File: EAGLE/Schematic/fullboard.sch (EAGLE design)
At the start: 91 parts, among them CN1 B4B-XH-A, CN2 B4B-XH-A, IC1 IFX007T, IC2 IFX007T, IC3 IFX007T, IC4 IFX007T, J1 10118193-0001LF, Q1 8MHz ±10ppm Crystal 18pF 80 O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, SW1 TR1-SPST, U1 ATXMEGA128A3U-AU, U2 FT232RL-REEL

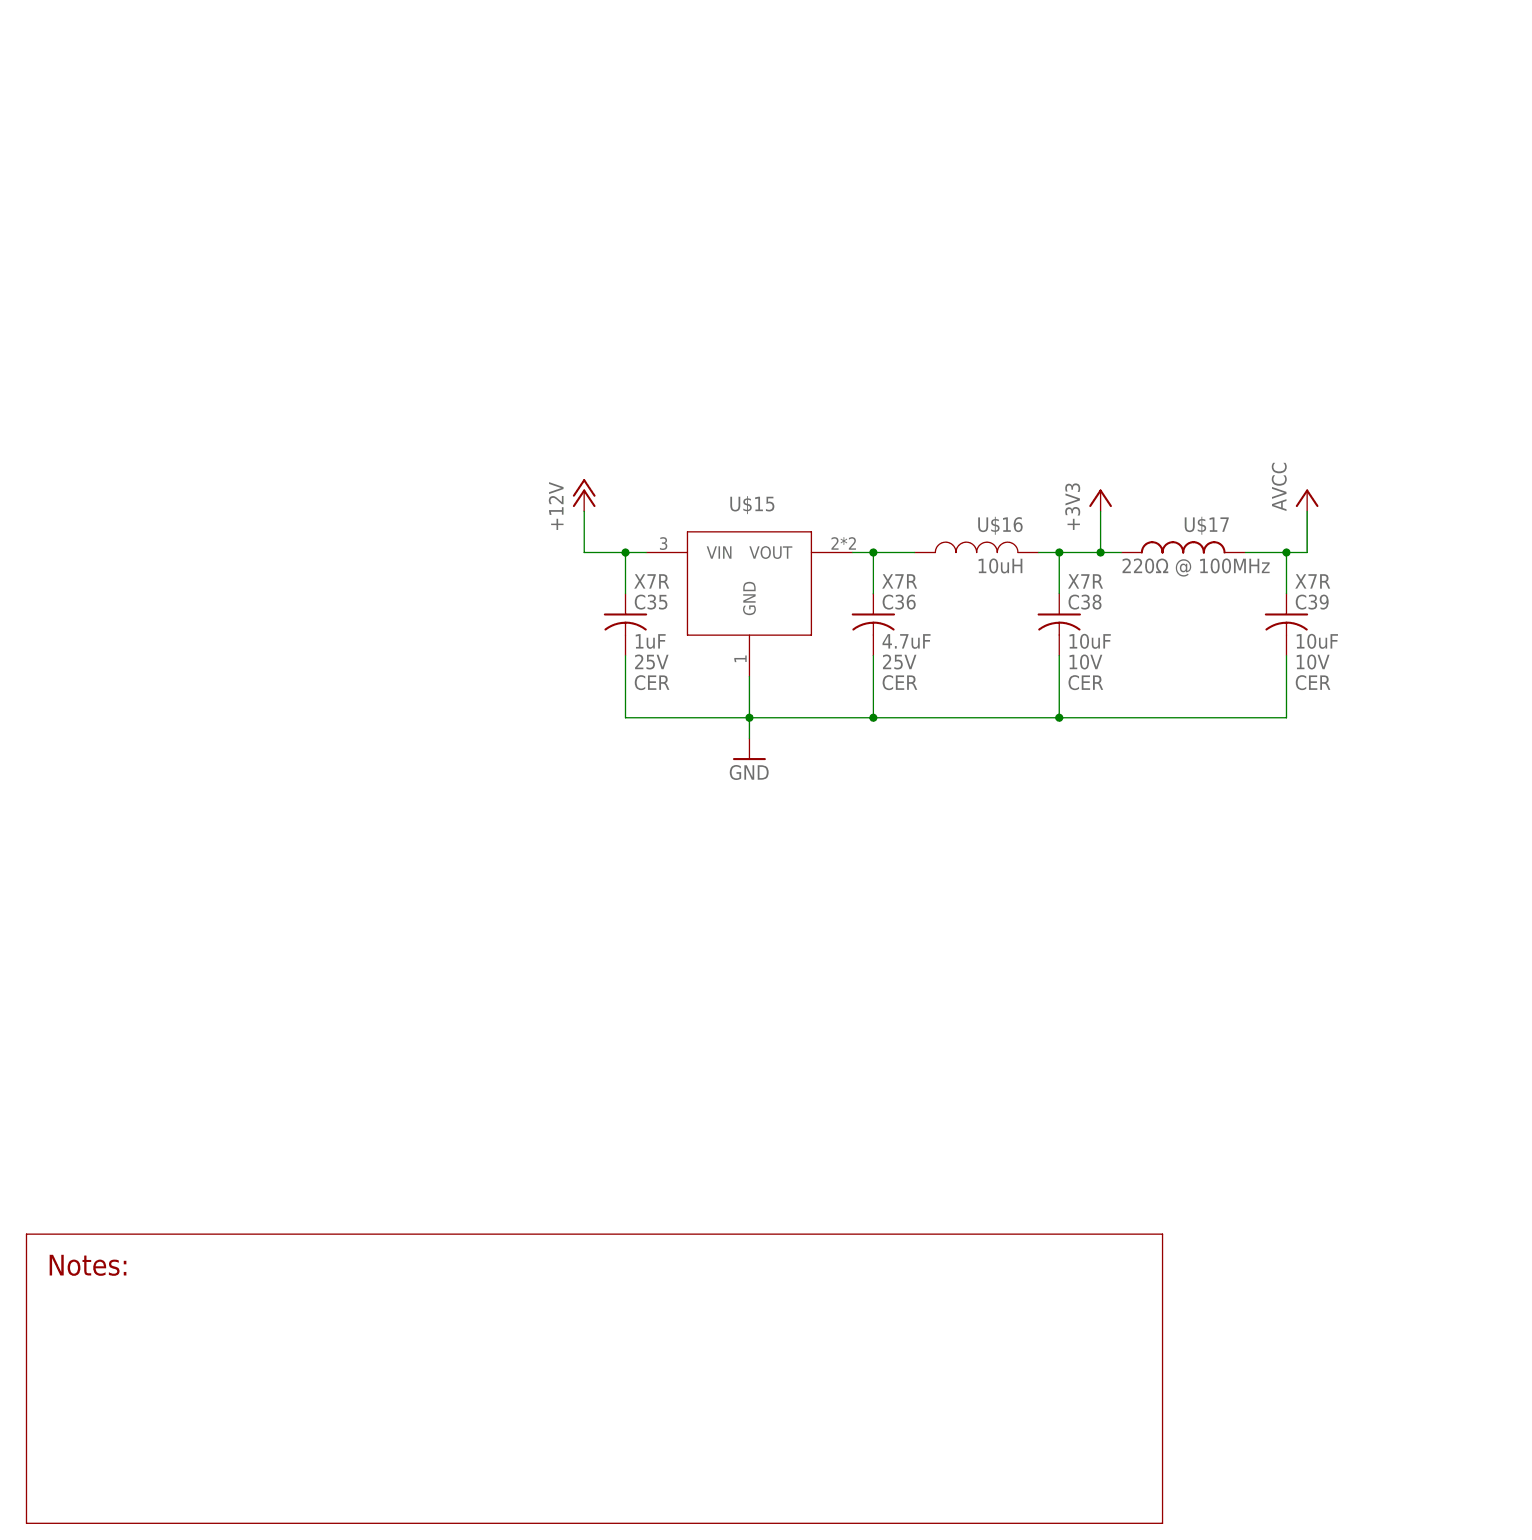
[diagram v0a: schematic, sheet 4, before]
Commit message: V0.1 of the board
Did some more signal routing, added a connector for the mouse, added a simple 5V regulator circuit
Still need:
* Edge sensor connectors
* Footprint 2x check
* Probably some other things
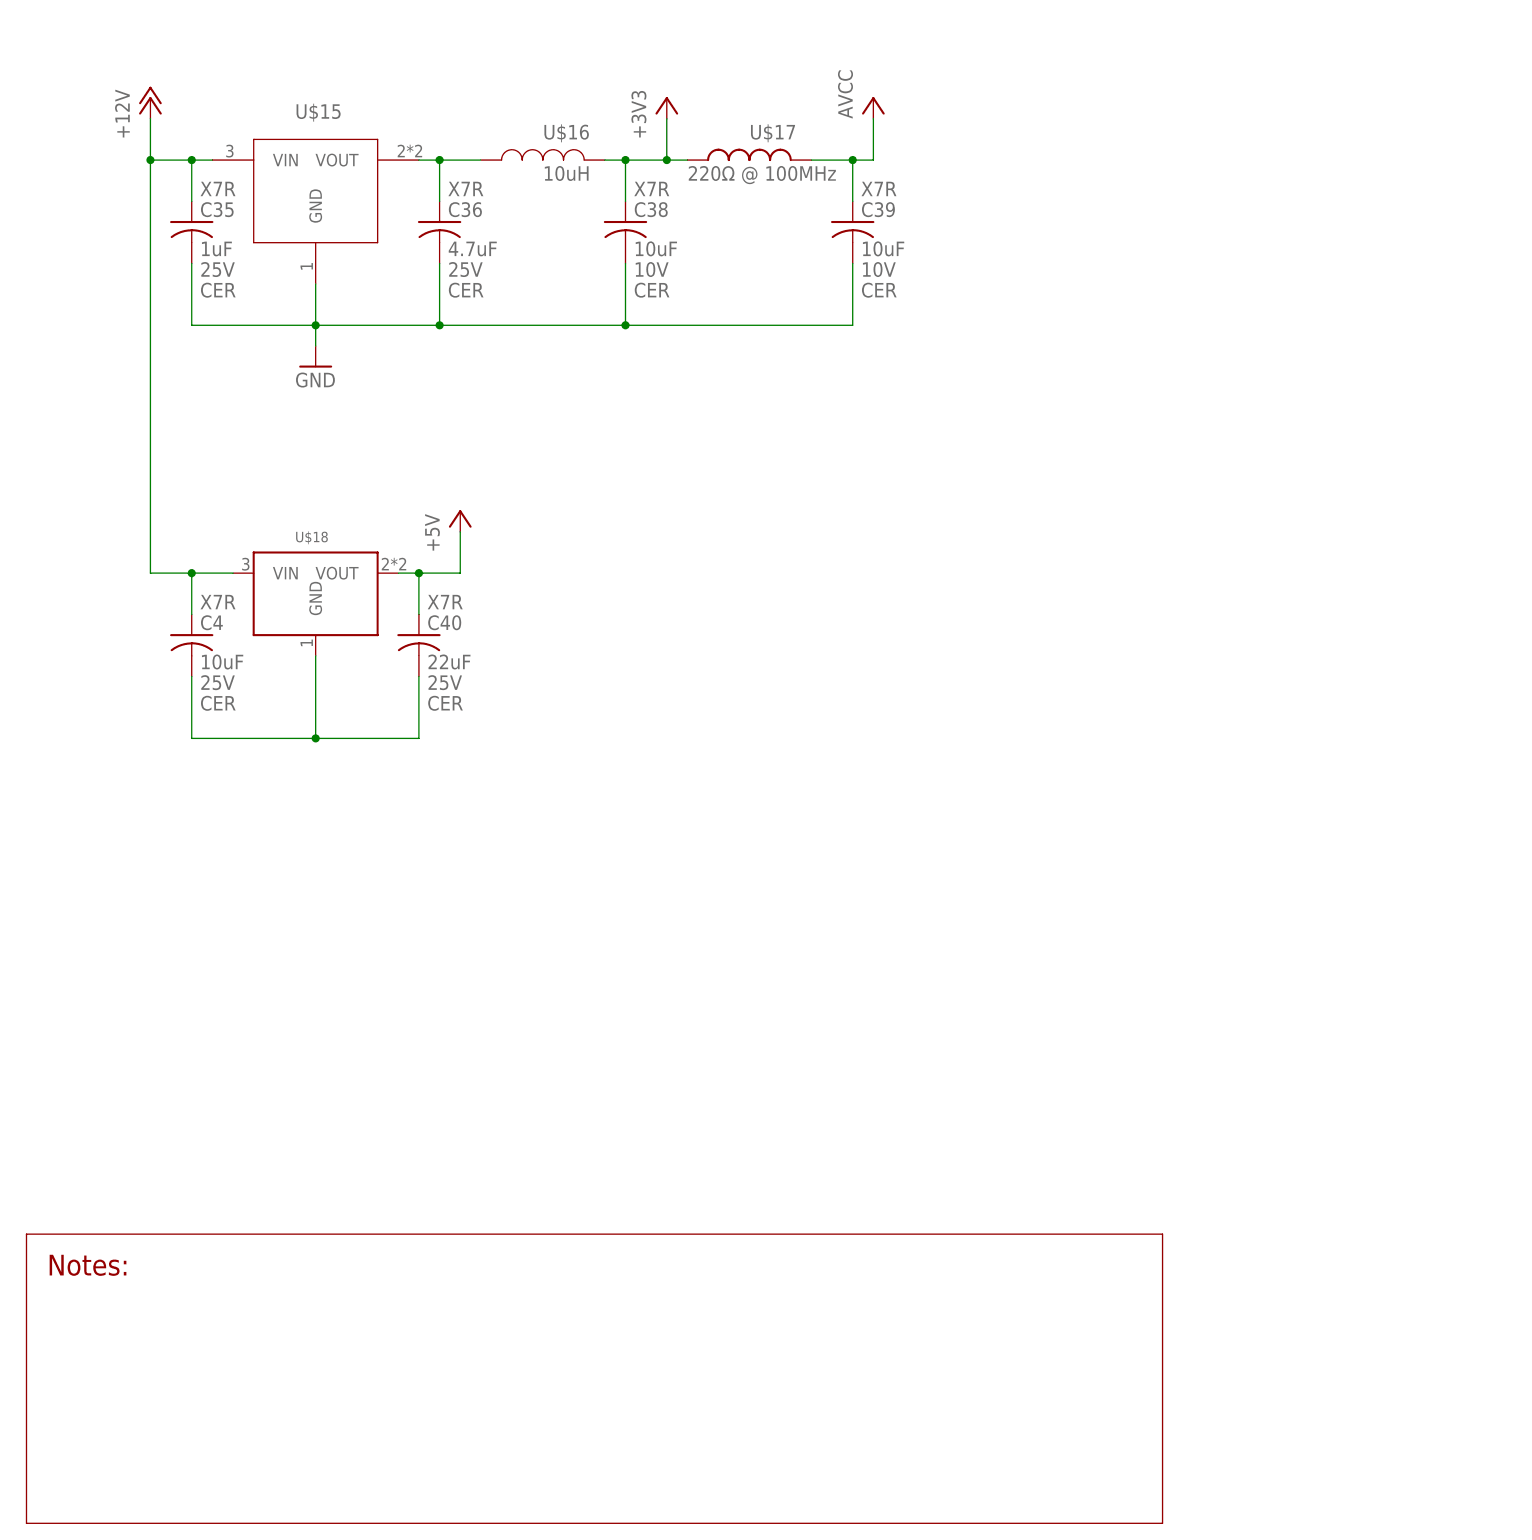
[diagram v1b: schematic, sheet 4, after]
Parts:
- added C4: 10uF, rcl:C-USC1206
- added C40: 22uF, rcl:C-USC1210
- added CN3: B4B-XH-A, jst:B4B-XH-A
- added U$18: AZ1117IH, SumBot:AZ1117IH
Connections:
- net N$36 renamed VCCIO
- removed net RX_MSE: U1A.PC5
- removed net TX_MSE: U1A.PC6
- new net N$1: C4.2, C40.2, U$18.GND
- new net TX/RX_MSE: CN3.3, U1A.PC5, U1A.PC6
- new net USB_PWR: C30.1, C31.1, C32.1, J1.VUSB, U2.VCC
- net +12V: now also C4.1, U$18.VIN
- net +5V: now also C40.1, CN3.1, U$18.VOUT; no longer C30.1, C31.1, C32.1, J1.VUSB, U2.VCC
- net GND: now also CN3.4
- net XCK_MSE: now also CN3.2
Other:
- moved on the sheet: C35, C36, C38, C39, U$15, U$16, U$17

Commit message: V0.2
Added Edge Detection and reconfigured other pins
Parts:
- added CN4, CN5, CN6, CN7, CN8, CN9: S4B-ZR, jst:S4B-ZR
- CN1, CN2, CN3: value B4B-XH-A -> B4B-ZR; device jst:B4B-XH-A -> jst:B4B-ZR
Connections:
- new net EDGE_CTRL: CN4.4, CN5.4, CN6.4, CN7.4, CN8.4, CN9.4, U1A.PC0
- net +3V3: now also CN4.2, CN5.2, CN6.2, CN7.2, CN8.2, CN9.2
- net BCK_A: now also U1A.PE5; no longer U1A.PD1
- net BCK_B: now also U1A.PE2; no longer U1A.PD3
- net EA_A: now also U1A.PF6; no longer U1A.PF4
- net EA_B: now also U1A.PD1; no longer U1A.PF1
- net EB_A: now also U1A.PF7; no longer U1A.PF5
- net EB_B: now also U1A.PD0; no longer U1A.PF2
- net EDGE_A: now also CN4.1, U1A.PA2; no longer U1A.PA0
- net EDGE_B: now also CN5.1, U1A.PA3; no longer U1A.PA1
- net EDGE_C: now also CN6.1, U1A.PA4; no longer U1A.PA2
- net EDGE_D: now also CN7.1, U1A.PA5; no longer U1A.PA3
- net EDGE_E: now also CN8.1, U1A.PA6; no longer U1A.PA4
- net EDGE_F: now also CN9.1, U1A.PA7; no longer U1A.PA5
- net EN_A: now also U1A.PE6; no longer U1A.PF3
- net EN_B: now also U1A.PE1; no longer U1A.PF0
- net FWD_A: now also U1A.PE4; no longer U1A.PD0
- net FWD_B: now also U1A.PE3; no longer U1A.PD2
- net GND: now also CN4.3, CN5.3, CN6.3, CN7.3, CN8.3, CN9.3
- net TX/RX_MSE: now also U1A.PC7; no longer U1A.PC5
- net XCK_MSE: now also U1A.PC5; no longer U1A.PC4
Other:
- note added: "EDGE_(A-F) represent the sensor output voltage which ranges from 0 V to Vcc provided to sensor EDGE_CTRL is the LED emitter current control pin"
